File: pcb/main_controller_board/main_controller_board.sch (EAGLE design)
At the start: 52 parts, among them K1 61400416021, U1 CAMERA0, U2 CAMERA1, U3 DMG1012T, U4 TENDA_P200, U5 PAM2306, U6 AP7115-XXSEG

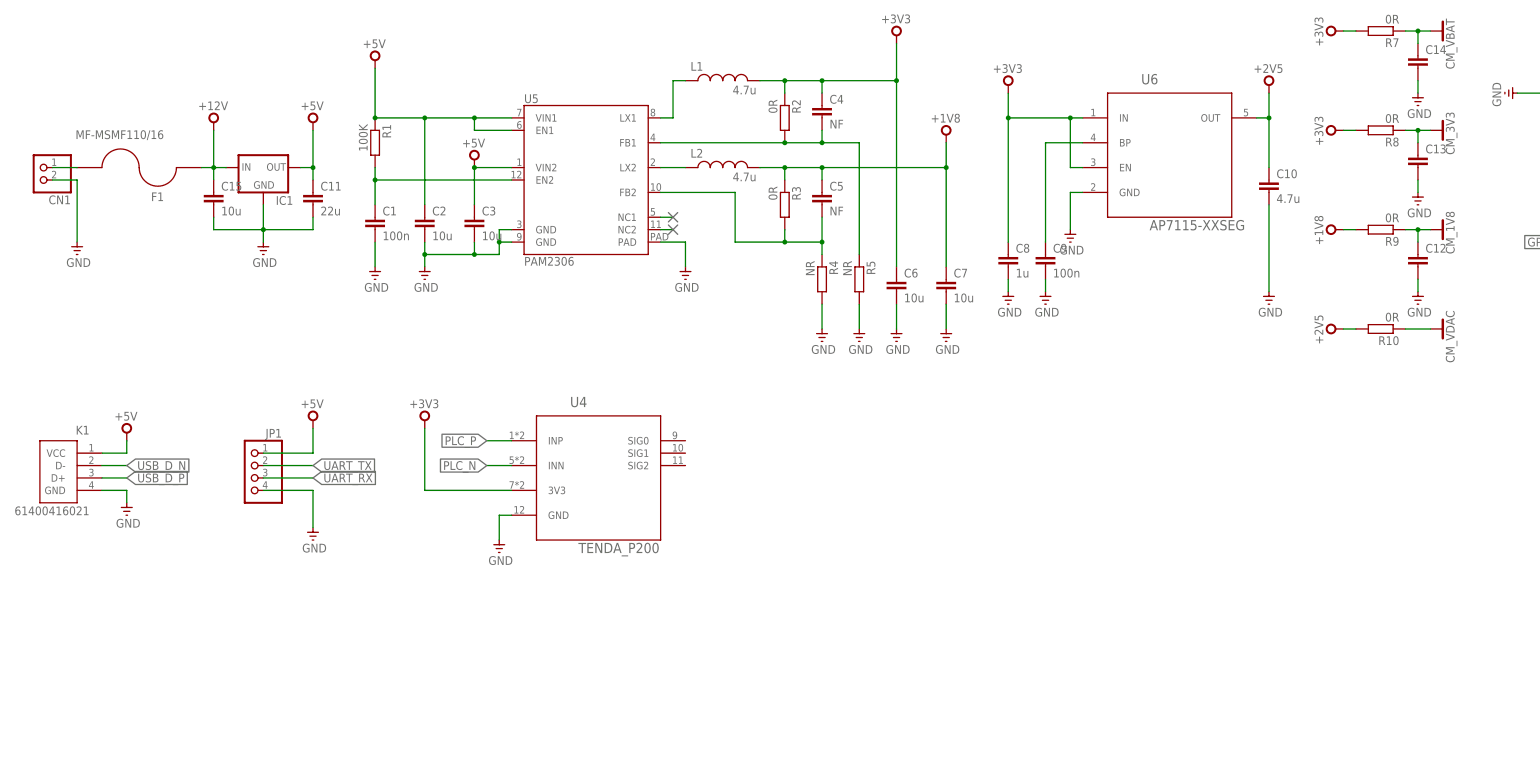
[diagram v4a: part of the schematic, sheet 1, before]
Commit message: 0.5mm clearance
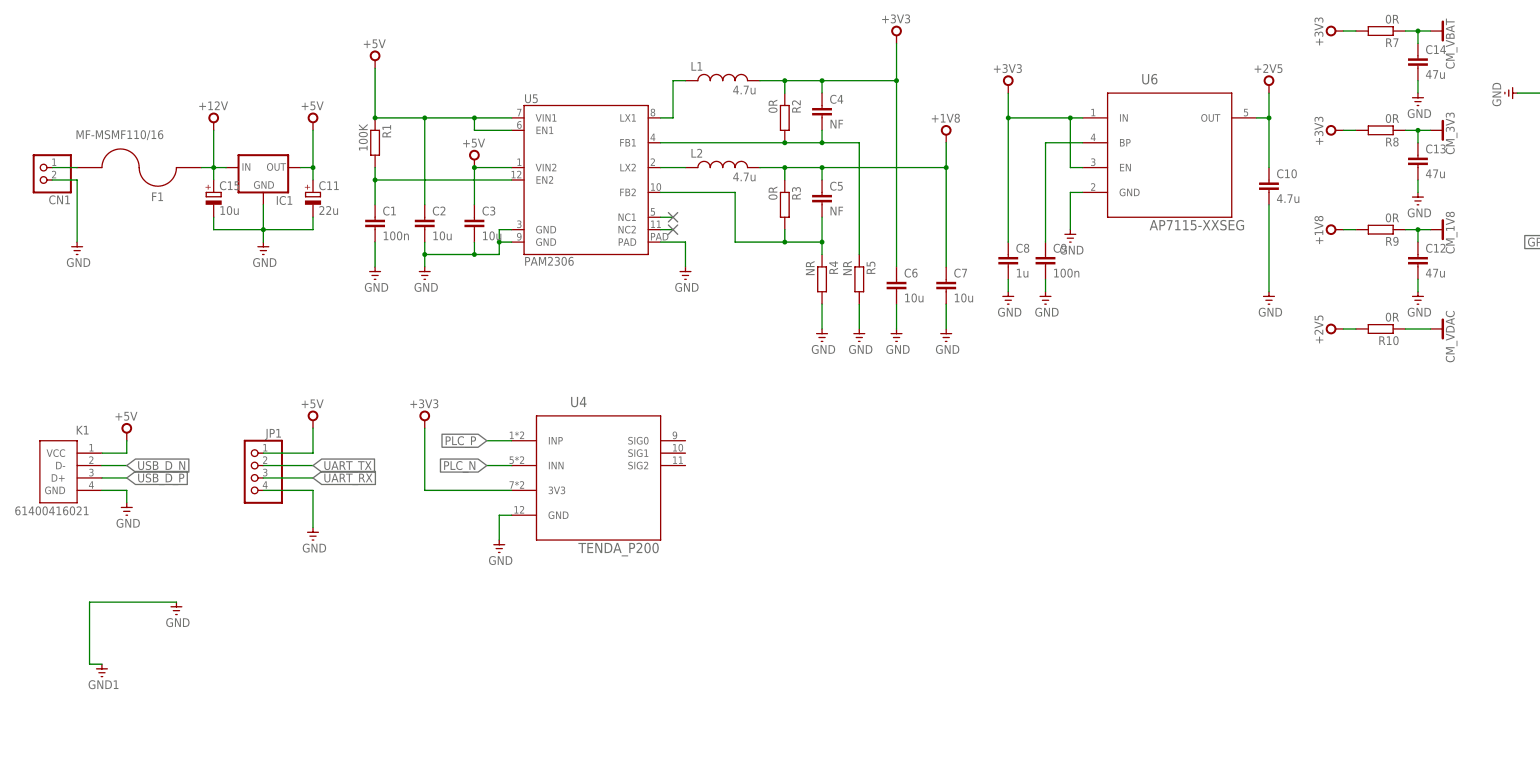
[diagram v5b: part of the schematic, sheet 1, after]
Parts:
- C11, C15: device resistor:C-EUC1206 -> resistor:CPOL-EU153CLV-0405
- C12, C13, C14: value (none) -> 47u
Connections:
- net +12V: now also C15.+; no longer C15.1
- net +5V: now also C11.+; no longer C11.1
- net GND: now also C11.-, C15.-; no longer C11.2, C15.2
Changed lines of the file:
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@@
 <part name="GND13" library="supply" deviceset="GND" device=""/>
 <part name="GND14" library="supply" deviceset="GND" device=""/>
-<part name="C11" library="resistor" deviceset="C-EU" device="C1206" value="22u"/>
+<part name="C11" library="resistor" deviceset="CPOL-EU" device="153CLV-0405" value="22u"/>
 <part name="V9" library="supply" deviceset="+12V" device=""/>
 <part name="JP1" library="pinhead" deviceset="PINHD-1X4" device=""/>
@@
 <part name="GND18" library="supply" deviceset="GND" device=""/>
 <part name="GND19" library="supply" deviceset="GND" device=""/>
-<part name="C12" library="resistor" deviceset="C-EU" device="C1206"/>
-<part name="C13" library="resistor" deviceset="C-EU" device="C1206"/>
-<part name="C14" library="resistor" deviceset="C-EU" device="C1206"/>
+<part name="C12" library="resistor" deviceset="C-EU" device="C1206" value="47u"/>
+<part name="C13" library="resistor" deviceset="C-EU" device="C1206" value="47u"/>
+<part name="C14" library="resistor" deviceset="C-EU" device="C1206" value="47u"/>
 <part name="R7" library="resistor" deviceset="R-EU_" device="R0805" value="0R"/>
 <part name="R8" library="resistor" deviceset="R-EU_" device="R0805" value="0R"/>
@@
 <part name="GND16" library="supply" deviceset="GND" device=""/>
 <part name="V11" library="supply" deviceset="+5V" device=""/>
-<part name="C15" library="resistor" deviceset="C-EU" device="C1206" value="10u"/>
+<part name="C15" library="resistor" deviceset="CPOL-EU" device="153CLV-0405" value="10u"/>
+<part name="GND26" library="supply" deviceset="GND" device=""/>
+<part name="GND30" library="supply" deviceset="GND1" device=""/>
 </parts>
 <sheets>
@@
 <instance part="V11" gate="1" x="30.48" y="160.02"/>
 <instance part="C15" gate="G$1" x="48.26" y="208.28"/>
+<instance part="GND26" gate="1" x="40.64" y="121.92"/>
+<instance part="GND30" gate="G$1" x="25.4" y="109.22"/>
 </instances>
 <busses>
@@
 <wire x1="66.04" y1="213.36" x2="68.58" y2="213.36" width="0.1524" layer="91"/>
 <wire x1="68.58" y1="213.36" x2="68.58" y2="220.98" width="0.1524" layer="91"/>
-<pinref part="C11" gate="G$1" pin="1"/>
+<pinref part="C11" gate="G$1" pin="+"/>
 <wire x1="68.58" y1="213.36" x2="68.58" y2="210.82" width="0.1524" layer="91"/>
 <junction x="68.58" y="213.36"/>
@@
 <pinref part="GND14" gate="1" pin="GND"/>
 <wire x1="58.42" y1="205.74" x2="58.42" y2="200.66" width="0.1524" layer="91"/>
-<pinref part="C11" gate="G$1" pin="2"/>
+<pinref part="C11" gate="G$1" pin="-"/>
 <wire x1="58.42" y1="200.66" x2="58.42" y2="198.12" width="0.1524" layer="91"/>
 <wire x1="68.58" y1="203.2" x2="68.58" y2="200.66" width="0.1524" layer="91"/>
 <wire x1="68.58" y1="200.66" x2="58.42" y2="200.66" width="0.1524" layer="91"/>
 <junction x="58.42" y="200.66"/>
-<pinref part="C15" gate="G$1" pin="2"/>
+<pinref part="C15" gate="G$1" pin="-"/>
 <wire x1="48.26" y1="203.2" x2="48.26" y2="200.66" width="0.1524" layer="91"/>
 <wire x1="48.26" y1="200.66" x2="58.42" y2="200.66" width="0.1524" layer="91"/>
@@
 <wire x1="48.26" y1="220.98" x2="48.26" y2="213.36" width="0.1524" layer="91"/>
 <junction x="48.26" y="213.36"/>
-<pinref part="C15" gate="G$1" pin="1"/>
+<pinref part="C15" gate="G$1" pin="+"/>
 <wire x1="48.26" y1="210.82" x2="48.26" y2="213.36" width="0.1524" layer="91"/>
 </segment>
@@
 </segment>
 </net>
+<net name="GND1" class="0">
+<segment>
+<pinref part="GND26" gate="1" pin="GND"/>
+<wire x1="40.64" y1="124.46" x2="22.86" y2="124.46" width="0.1524" layer="91"/>
+<pinref part="GND30" gate="G$1" pin="GND1"/>
+<wire x1="25.4" y1="111.76" x2="22.86" y2="111.76" width="0.1524" layer="91"/>
+<wire x1="22.86" y1="111.76" x2="22.86" y2="124.46" width="0.1524" layer="91"/>
+</segment>
+</net>

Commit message: order
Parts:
- CN1: value (none) -> B2B-PH-K-S
- F1: value MF-MSMF110/16 -> MF-MSMF200
- IC1: value (none) -> V7805-1000
- JP1: value (none) -> 90131-0764; device pinhead:PINHD-1X4 -> pinhead:PINHD-2X4
- PCB1: value RPCM -> 1473005-4
- U1: value CAMERA0 -> SFW15R-1STE1LF
- U2: value CAMERA1 -> SFW15R-1STE1LF
- U5: value PAM2306 -> PAM2306AYPKE
- U6: value AP7115-XXSEG -> AP7115-25SEG
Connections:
- removed net EXT0: PCB1.63/GPIO18
- removed net EXT1: PCB1.65/GPIO19
- removed net UART_RX: JP1.3, PCB1.53/GPIO15
- removed net UART_TX: JP1.2, PCB1.51/GPIO14
- new net EXT0/UART1_TX: JP1.6, PCB1.70/GPIO40
- new net EXT1/UART1_RX: JP1.4, PCB1.72/GPIO41
- new net UART0_RX: JP1.5, PCB1.53/GPIO15
- new net UART0_TX: JP1.3, PCB1.51/GPIO14
- net +5V: now also JP1.2
- net GND: now also JP1.7, JP1.8; no longer JP1.4
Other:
- moved on the sheet: U4
